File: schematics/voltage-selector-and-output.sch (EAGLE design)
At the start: 24 parts, among them IC2 ATTINY85, IC3 MCP41010P, IC4 5V, IC5 MIC2941, X1 USB-A-H

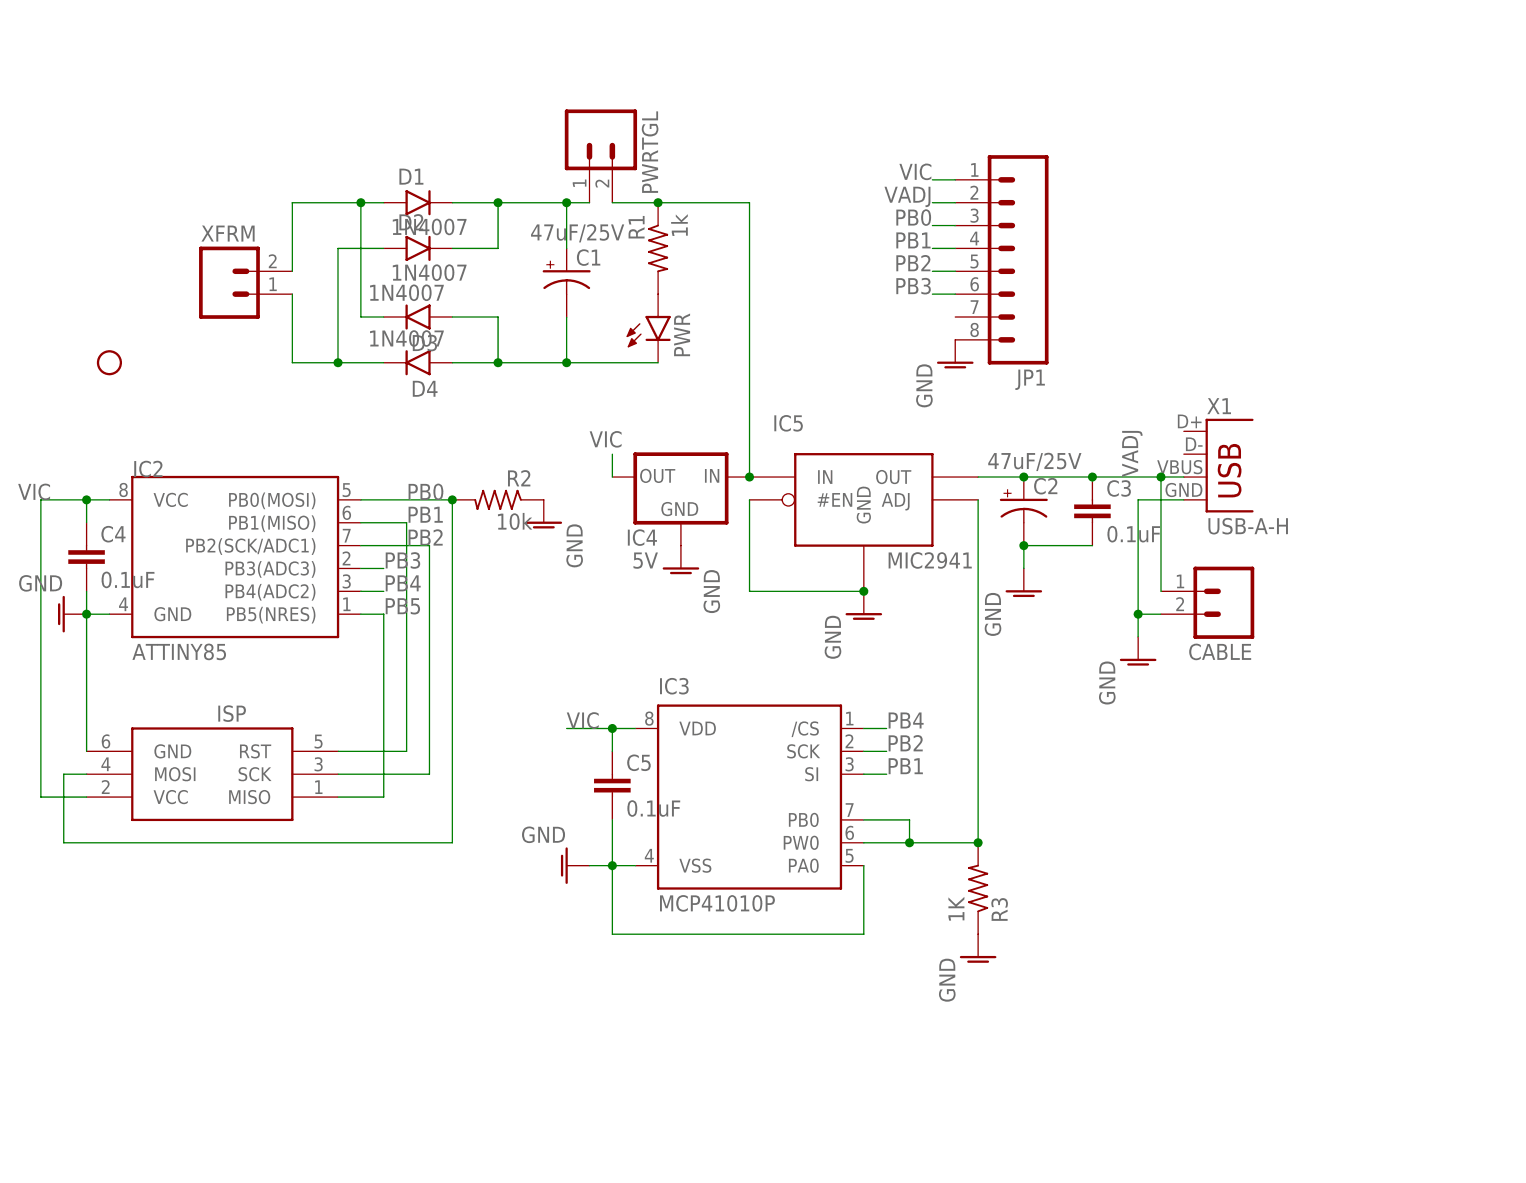
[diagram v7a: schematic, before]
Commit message: Decided to give SMT another chance
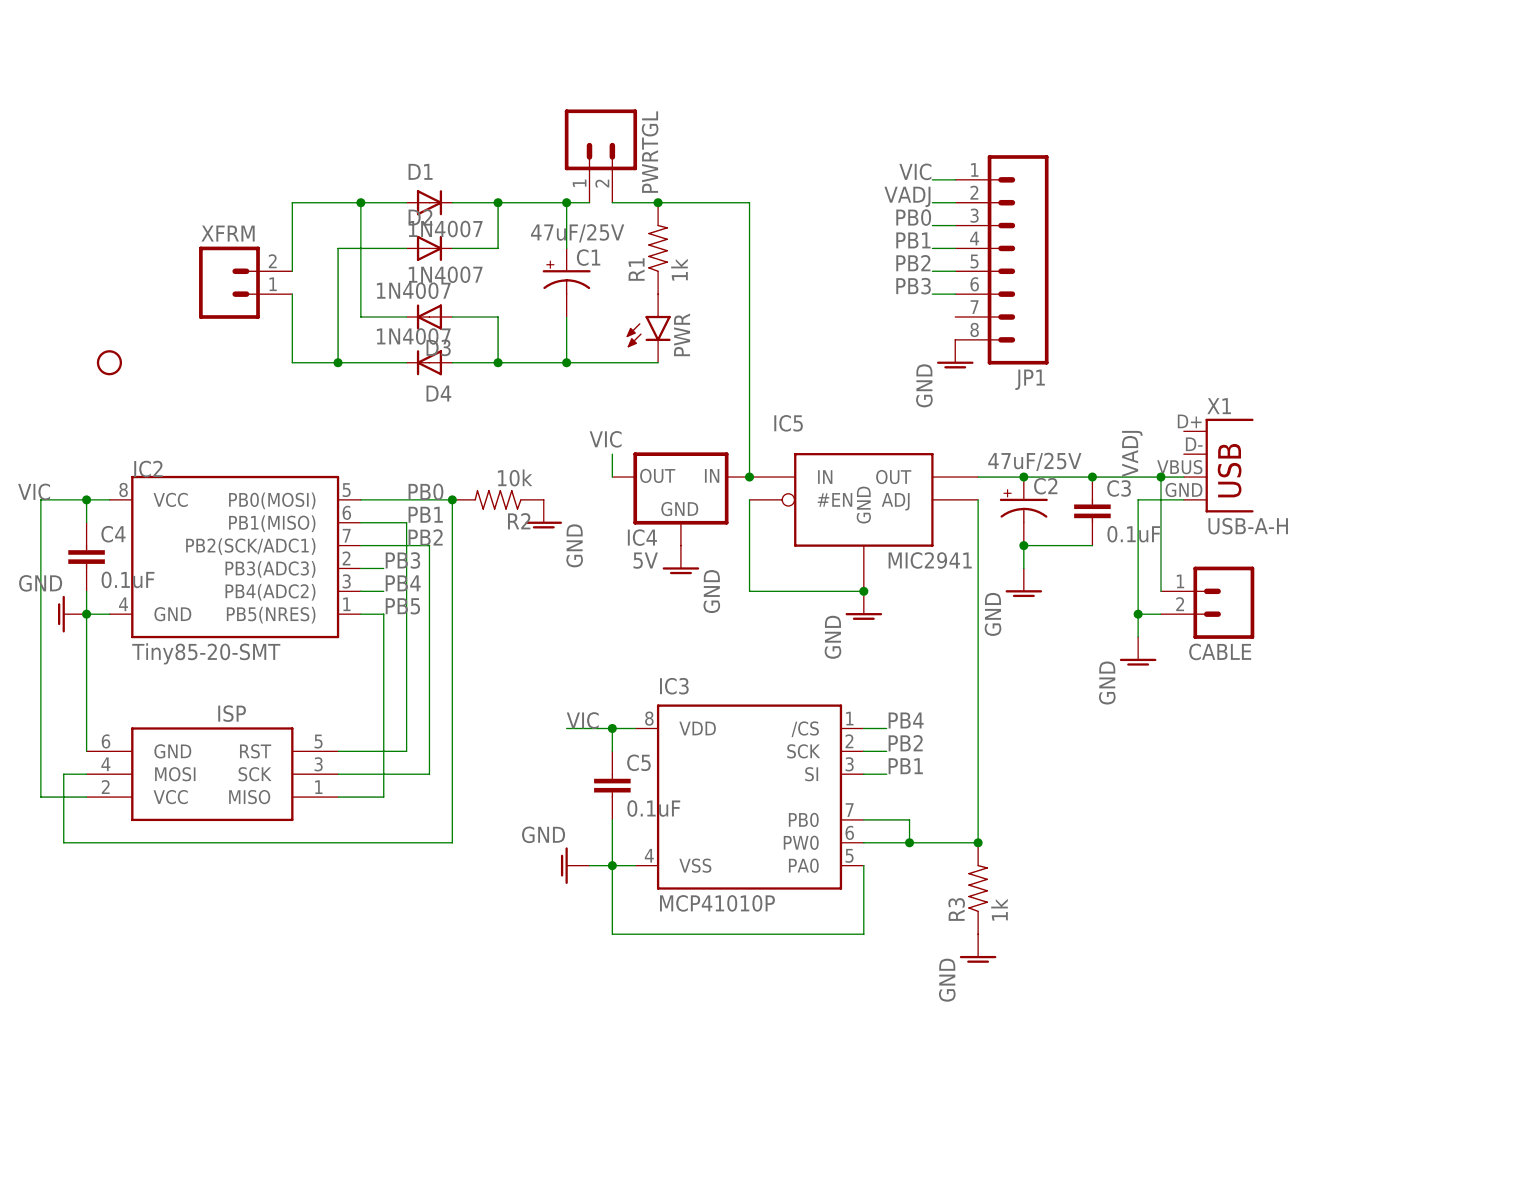
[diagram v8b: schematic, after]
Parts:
- C3, C4, C5: device SparkFun-Capacitors:CAPPTH -> SparkFun-Capacitors:1.0UF-25V-+80/-20(0805)"
- D1, D2, D3, D4: device gm-diodes:1N400X.3 -> diode:GF1
- IC2: value ATTINY85 -> Tiny85-20-SMT; device SparkFun:ATTINY13DIP -> SparkFun-DigitalIC:ATTINY45TINY85-20-SMT
- R1, R2: device rcl-ez:R-US_0207/5V -> SparkFun-Resistors:0.22OHM-1/4W-1%(0805)
- R3: value 1K -> 1k; device rcl-ez:R-US_0207/5V -> SparkFun-Resistors:0.22OHM-1/4W-1%(0805)
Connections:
- removed net N$10: PWR.A, R1.2
- new net N$3: PWR.A, R1.1
- net VCC: now also R1.2; no longer R1.1
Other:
- moved on the sheet: R1, R2
